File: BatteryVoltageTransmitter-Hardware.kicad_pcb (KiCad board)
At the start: 2 copper layers, 51.8 x 54.4 mm, 4 parts, among them U1 MSP_EXP432P401R_Launchpad_Shi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, U2 Raspberry_Pi

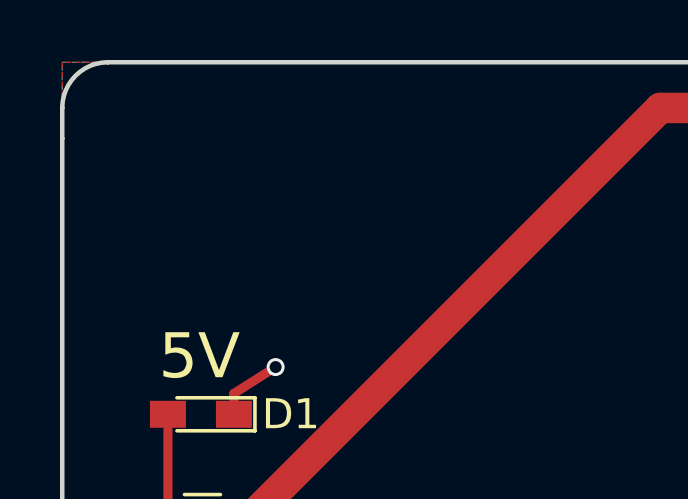
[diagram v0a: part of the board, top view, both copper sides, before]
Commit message: Added MRDT Logo and Cleaned Schematic
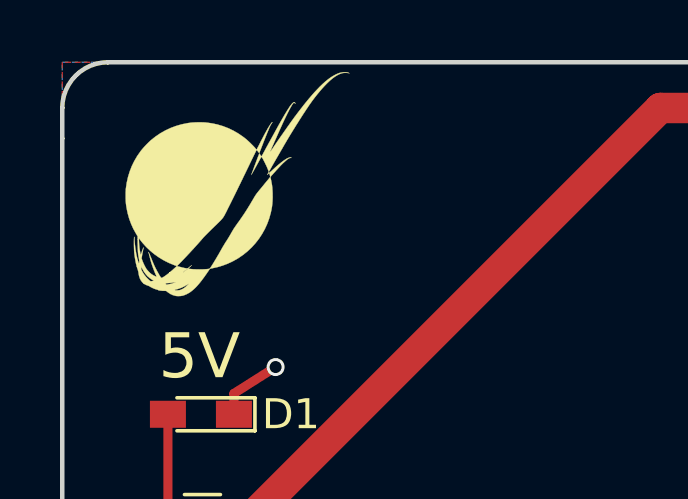
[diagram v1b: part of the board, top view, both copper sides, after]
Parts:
- added S1: MRDT_Logo, MRDT-Silkscreens:MRDT_Logo_7.5mm, F.Cu at (131.8, 63.5)

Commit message: Logos updated
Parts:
- added S2: Logo_or_Signature, MRDT-Silkscreens:Atlas_Logo_28.6mmX37.3mm, F.Cu at (148.6, 82.0)
- S1: value MRDT_Logo -> Logo_or_Signature
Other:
- board text added: "Mars Rover Design Team"
- board text added: "Missouri S&T Battery Voltage Transmitter Rev. 1 2018 Timothy Barnett Jacob Lipina"
- board text removed: "Mars Rover Design Team Missouri S&T Battery Voltage Transmitter Rev. 1 2018 Timothy Barnett Jacob Lipina"
